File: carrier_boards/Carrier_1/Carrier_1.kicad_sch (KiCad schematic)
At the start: 21 parts, among them J1 CH1, J10 CH1, J11 CH1, J12 CH1, J13 CH1, J14 CH1, J2 CH1, J3 CH1, J4 CH1, J5 CH1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

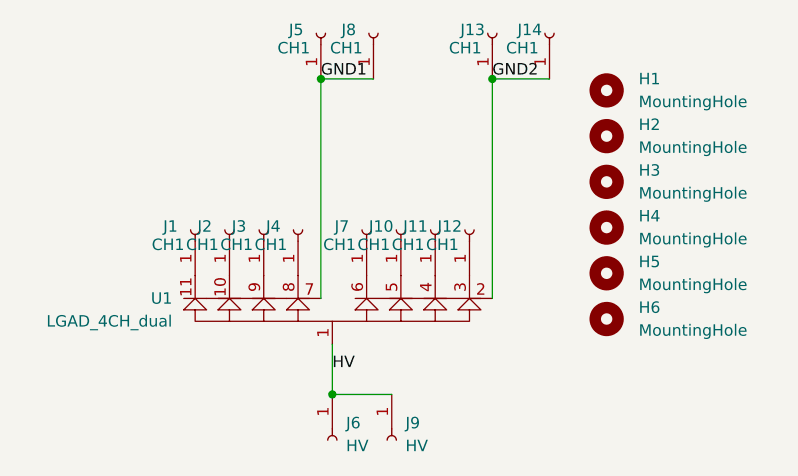
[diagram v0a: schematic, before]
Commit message: Converted files to KiCAD 7
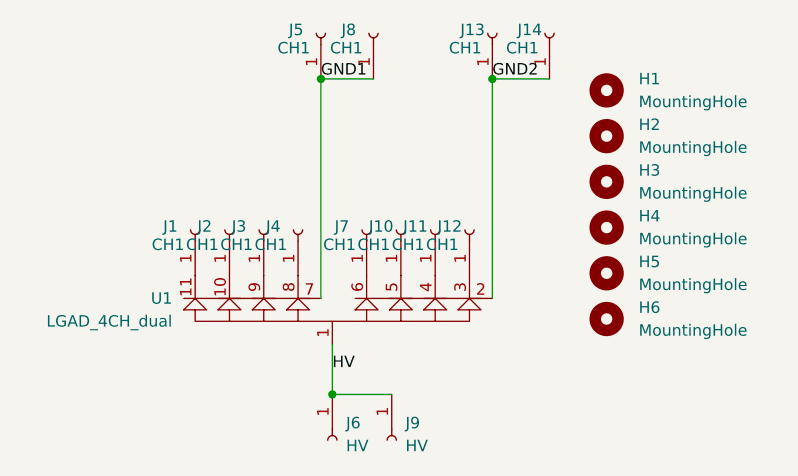
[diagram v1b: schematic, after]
